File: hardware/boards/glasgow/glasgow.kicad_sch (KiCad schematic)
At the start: 95 parts, among them J1 USB_C_USB2.0, SW1 RST, U1 CY7C68013A-56LTX, U15 TPD3S014, U2 CAT24M01X, U3 BL24C256A-SFRC, U30 ICE40HX8K-BG121, U36 TLV73312PQDRVR, U7 APX811-40UG-7, U8 TLV75533PDRVR, Y1 24M

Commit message: revC3: Hid U12&U21 labels. Corrected APX 1b2 key.
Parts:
- U7: 1b2-bom-key ic-cat811jtbi -> ic-apx811-40ug-7
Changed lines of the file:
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@@
       (effects (font (size 1.27 1.27)) hide)
     )
-    (property "1b2-bom-key" "ic-cat811jtbi" (id 4) (at 220.98 91.44 0)
+    (property "1b2-bom-key" "ic-apx811-40ug-7" (id 4) (at 220.98 91.44 0)
       (effects (font (size 1.27 1.27)) hide)
     )

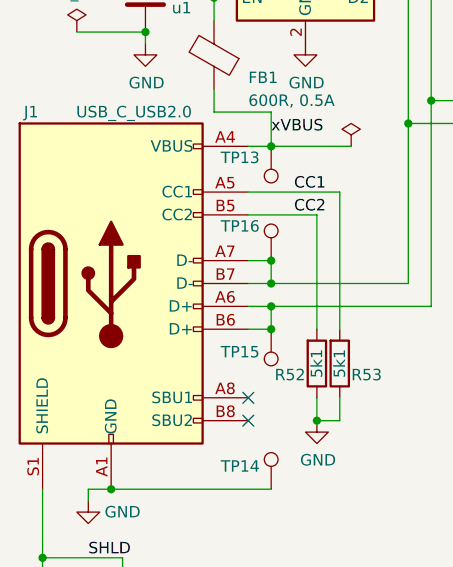
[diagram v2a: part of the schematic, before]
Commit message: revC3: Final cleanups before production.
* Changed 3D models to step so the 3D model can be exported for
  enclosure CAD.
* Changed silk and stop colors to match 1BitSquared production boards
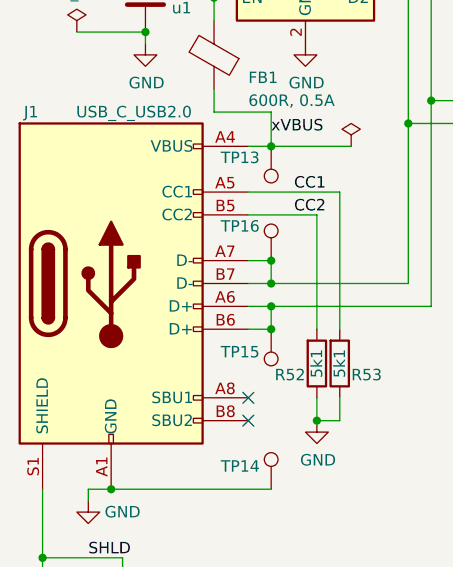
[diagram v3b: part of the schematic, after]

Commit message: revC3: Corrected U2 (CAT24M01) part number.
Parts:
- U2: MPN CAT24M01XI-T2 -> CAT24M01YI−GT3
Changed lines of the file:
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@@
       (effects (font (size 1.27 1.27)) hide)
     )
-    (property "MPN" "CAT24M01XI-T2" (at 8.89 355.6 0)
+    (property "MPN" "CAT24M01YI−GT3" (at 8.89 355.6 0)
       (effects (font (size 1.27 1.27)) hide)
     )

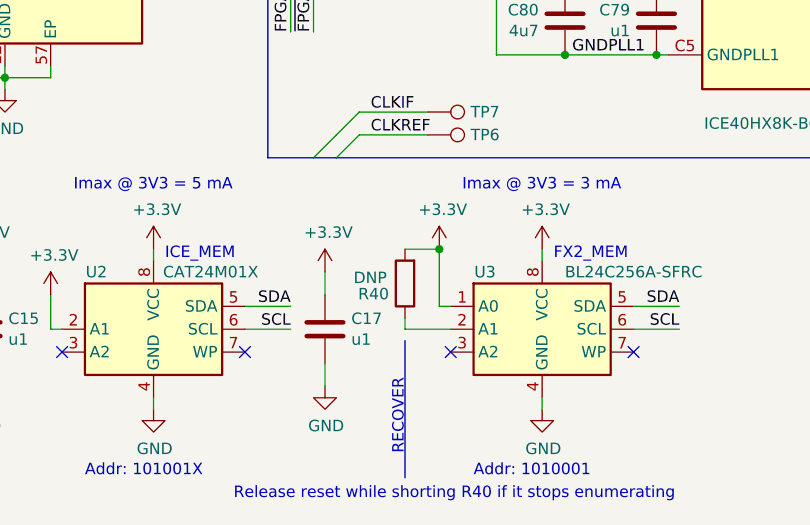
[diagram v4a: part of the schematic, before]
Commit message: revC3: Use the new KiCad DNP flag for the DNP parts.
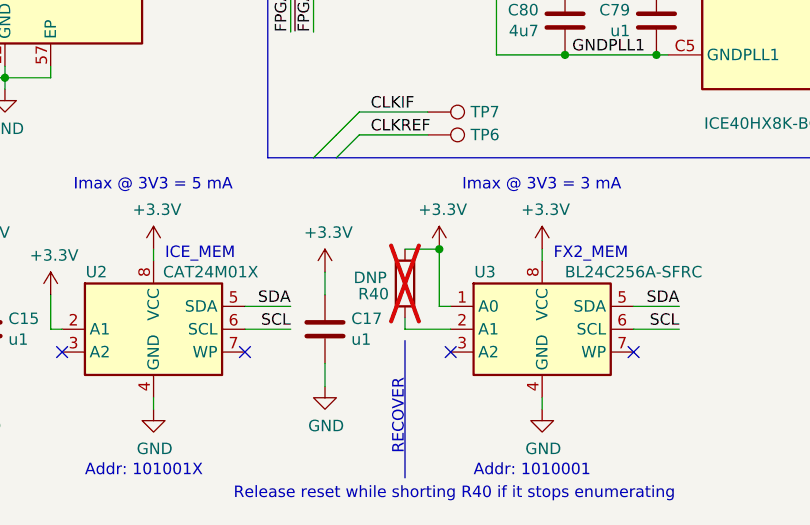
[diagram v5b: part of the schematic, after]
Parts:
- R40: now not fitted; now left out of the parts list
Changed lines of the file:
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@@
   )
   (symbol (lib_id "Device:R") (at 134.62 172.72 180) (unit 1)
-    (in_bom yes) (on_board yes) (dnp no)
+    (in_bom no) (on_board yes) (dnp yes)
     (property "Reference" "R40" (at 132.842 173.8884 0)
       (effects (font (size 1.27 1.27)) (justify left))

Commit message: revC3: Marked non schematic/bom parts correctly.
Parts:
- MK1, MK2, MK3, MK4, TP1, TP10, TP11, TP12, TP13, TP14, TP15, TP16, TP17, TP2, TP3, TP4, TP5, TP6, TP7, TP8, TP9: now left out of the parts list
- R40: now in the parts list
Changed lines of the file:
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@@
   )
   (symbol (lib_id "Mechanical:MountingHole_Pad") (at 15.24 186.69 0) (unit 1)
-    (in_bom yes) (on_board yes) (dnp no)
+    (in_bom no) (on_board yes) (dnp no)
     (property "Reference" "MK1" (at 13.97 181.61 0)
       (effects (font (size 1.27 1.27)) (justify left))
@@
   )
   (symbol (lib_id "Mechanical:MountingHole_Pad") (at 20.32 186.69 0) (unit 1)
-    (in_bom yes) (on_board yes) (dnp no)
+    (in_bom no) (on_board yes) (dnp no)
     (property "Reference" "MK2" (at 19.05 181.61 0)
       (effects (font (size 1.27 1.27)) (justify left))
@@
   )
   (symbol (lib_id "Mechanical:MountingHole_Pad") (at 25.4 186.69 0) (unit 1)
-    (in_bom yes) (on_board yes) (dnp no)
+    (in_bom no) (on_board yes) (dnp no)
     (property "Reference" "MK3" (at 24.13 181.61 0)
       (effects (font (size 1.27 1.27)) (justify left))
@@
   )
   (symbol (lib_id "Mechanical:MountingHole_Pad") (at 30.48 186.69 0) (unit 1)
-    (in_bom yes) (on_board yes) (dnp no)
+    (in_bom no) (on_board yes) (dnp no)
     (property "Reference" "MK4" (at 29.21 181.61 0)
       (effects (font (size 1.27 1.27)) (justify left))
@@
   )
   (symbol (lib_id "Connector:TestPoint") (at 58.42 85.09 270) (unit 1)
-    (in_bom yes) (on_board yes) (dnp no)
+    (in_bom no) (on_board yes) (dnp no)
     (property "Reference" "TP1" (at 59.69 82.55 90)
       (effects (font (size 1.27 1.27)) (justify left))
@@
   )
   (symbol (lib_id "Connector:TestPoint") (at 264.16 144.78 270) (unit 1)
-    (in_bom yes) (on_board yes) (dnp no)
+    (in_bom no) (on_board yes) (dnp no)
     (property "Reference" "TP2" (at 267.97 142.24 90)
       (effects (font (size 1.27 1.27)))
@@
   )
   (symbol (lib_id "Connector:TestPoint") (at 264.16 118.11 270) (unit 1)
-    (in_bom yes) (on_board yes) (dnp no)
+    (in_bom no) (on_board yes) (dnp no)
     (property "Reference" "TP3" (at 267.97 115.57 90)
       (effects (font (size 1.27 1.27)))
@@
   )
   (symbol (lib_id "Connector:TestPoint") (at 67.31 130.81 180) (unit 1)
-    (in_bom yes) (on_board yes) (dnp no)
+    (in_bom no) (on_board yes) (dnp no)
     (property "Reference" "TP4" (at 68.58 137.16 0)
       (effects (font (size 1.27 1.27)) (justify left))
@@
   )
   (symbol (lib_id "Connector:TestPoint") (at 69.85 130.81 180) (unit 1)
-    (in_bom yes) (on_board yes) (dnp no)
+    (in_bom no) (on_board yes) (dnp no)
     (property "Reference" "TP5" (at 71.12 137.16 0)
       (effects (font (size 1.27 1.27)))
@@
   )
   (symbol (lib_id "Connector:TestPoint") (at 137.16 156.21 270) (mirror x) (unit 1)
-    (in_bom yes) (on_board yes) (dnp no)
+    (in_bom no) (on_board yes) (dnp no)
     (property "Reference" "TP6" (at 141.9098 156.21 90)
       (effects (font (size 1.27 1.27)) (justify left))
@@
   )
   (symbol (lib_id "Connector:TestPoint") (at 137.16 153.67 270) (mirror x) (unit 1)
-    (in_bom yes) (on_board yes) (dnp no)
+    (in_bom no) (on_board yes) (dnp no)
     (property "Reference" "TP7" (at 141.9098 153.67 90)
       (effects (font (size 1.27 1.27)) (justify left))
@@
   )
   (symbol (lib_id "Graphic:Logo_Open_Hardware_Large") (at 58.42 175.26 0) (unit 1)
-    (in_bom yes) (on_board yes) (dnp no)
+    (in_bom no) (on_board yes) (dnp no)
     (property "Reference" "#LOGO1" (at 58.42 162.56 0)
       (effects (font (size 1.27 1.27)) hide)
@@
   )
   (symbol (lib_id "Connector:TestPoint") (at 34.29 59.69 270) (unit 1)
-    (in_bom yes) (on_board yes) (dnp no)
+    (in_bom no) (on_board yes) (dnp no)
     (property "Reference" "TP8" (at 40.64 59.69 90)
       (effects (font (size 1.27 1.27)) (justify left))
@@
   )
   (symbol (lib_id "Connector:TestPoint") (at 34.29 62.23 270) (unit 1)
-    (in_bom yes) (on_board yes) (dnp no)
+    (in_bom no) (on_board yes) (dnp no)
     (property "Reference" "TP9" (at 40.64 62.23 90)
       (effects (font (size 1.27 1.27)) (justify left))
@@
   )
   (symbol (lib_id "Connector:TestPoint") (at 34.29 67.31 270) (unit 1)
-    (in_bom yes) (on_board yes) (dnp no)
+    (in_bom no) (on_board yes) (dnp no)
     (property "Reference" "TP10" (at 40.64 67.31 90)
       (effects (font (size 1.27 1.27)) (justify left))
@@
   )
   (symbol (lib_id "Connector:TestPoint") (at 34.29 69.85 270) (unit 1)
-    (in_bom yes) (on_board yes) (dnp no)
+    (in_bom no) (on_board yes) (dnp no)
     (property "Reference" "TP11" (at 40.64 69.85 90)
       (effects (font (size 1.27 1.27)) (justify left))
@@
   )
   (symbol (lib_id "Connector:TestPoint") (at 34.29 72.39 270) (unit 1)
-    (in_bom yes) (on_board yes) (dnp no)
+    (in_bom no) (on_board yes) (dnp no)
     (property "Reference" "TP12" (at 40.64 72.39 90)
       (effects (font (size 1.27 1.27)) (justify left))
@@
   )
   (symbol (lib_id "Connector:TestPoint") (at 40.64 130.81 180) (unit 1)
-    (in_bom yes) (on_board yes) (dnp no)
+    (in_bom no) (on_board yes) (dnp no)
     (property "Reference" "TP15" (at 39.37 133.35 0)
       (effects (font (size 1.27 1.27)) (justify left))
@@
   )
   (symbol (lib_id "Connector:TestPoint") (at 40.64 123.19 0) (unit 1)
-    (in_bom yes) (on_board yes) (dnp no)
+    (in_bom no) (on_board yes) (dnp no)
     (property "Reference" "TP16" (at 39.37 119.38 0)
       (effects (font (size 1.27 1.27)) (justify right))
@@
   )
   (symbol (lib_id "Connector:TestPoint") (at 40.64 110.49 180) (unit 1)
-    (in_bom yes) (on_board yes) (dnp no)
+    (in_bom no) (on_board yes) (dnp no)
     (property "Reference" "TP13" (at 39.37 111.76 0)
       (effects (font (size 1.27 1.27)) (justify left))
@@
   )
   (symbol (lib_id "Connector:TestPoint") (at 40.64 148.59 0) (unit 1)
-    (in_bom yes) (on_board yes) (dnp no)
+    (in_bom no) (on_board yes) (dnp no)
     (property "Reference" "TP14" (at 39.37 146.05 0)
       (effects (font (size 1.27 1.27)) (justify right))
@@
   )
   (symbol (lib_id "Connector:TestPoint") (at 34.29 64.77 270) (unit 1)
-    (in_bom yes) (on_board yes) (dnp no)
+    (in_bom no) (on_board yes) (dnp no)
     (property "Reference" "TP17" (at 40.64 64.77 90)
       (effects (font (size 1.27 1.27)) (justify left))
@@
   )
   (symbol (lib_id "Device:R") (at 134.62 172.72 180) (unit 1)
-    (in_bom no) (on_board yes) (dnp yes)
+    (in_bom yes) (on_board yes) (dnp yes)
     (property "Reference" "R40" (at 132.842 173.8884 0)
       (effects (font (size 1.27 1.27)) (justify left))

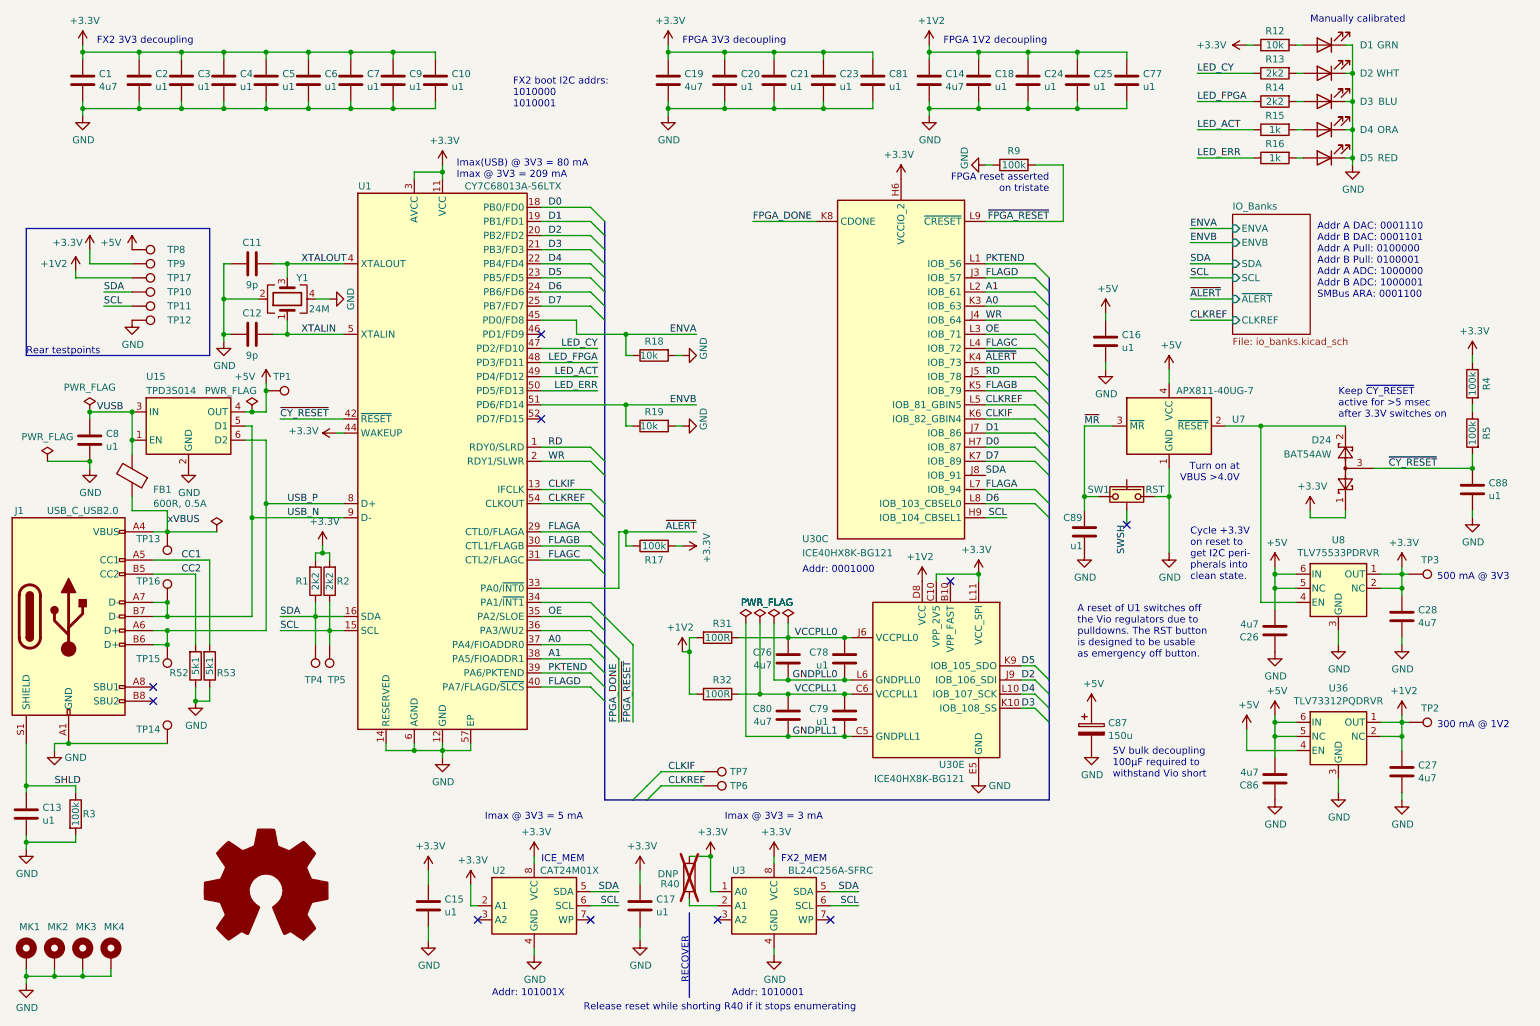
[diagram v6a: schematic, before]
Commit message: hardware: open & save with KiCAD 8.0.9
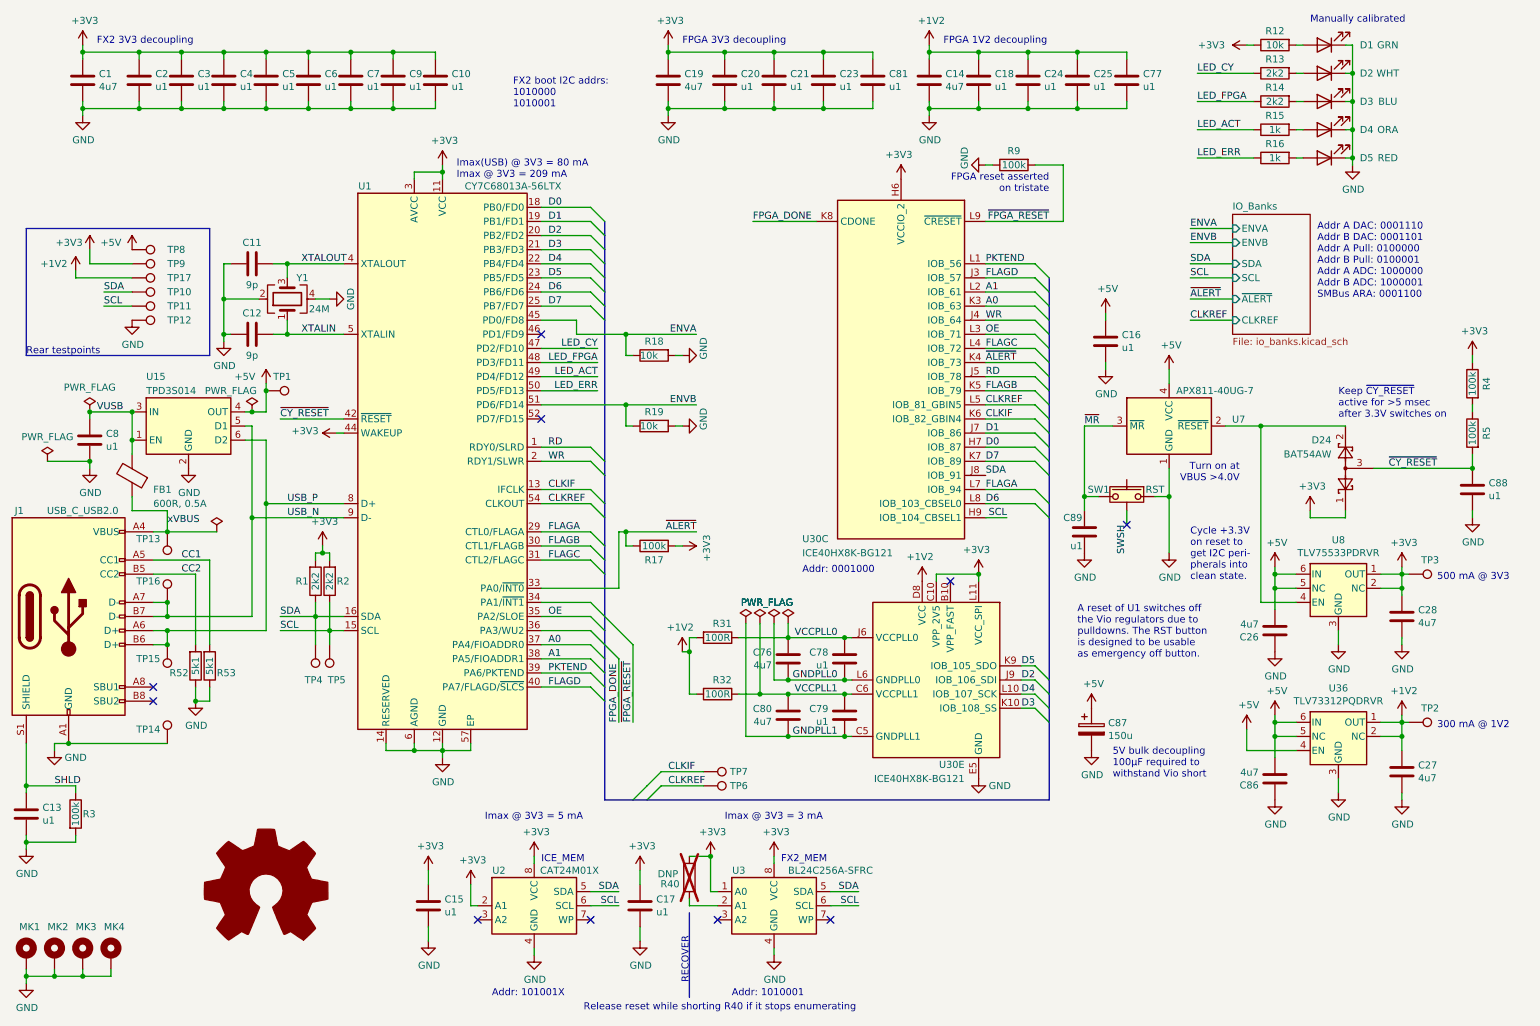
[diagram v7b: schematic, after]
